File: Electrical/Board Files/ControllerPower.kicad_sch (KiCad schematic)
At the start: 42 parts, among them J1 Conn_01x02_Female, Q1 PJA3411, Q2 PJA3411, SW11 SW_DIP_x01, U1 TPS63020, U2 BQ25050DQCR

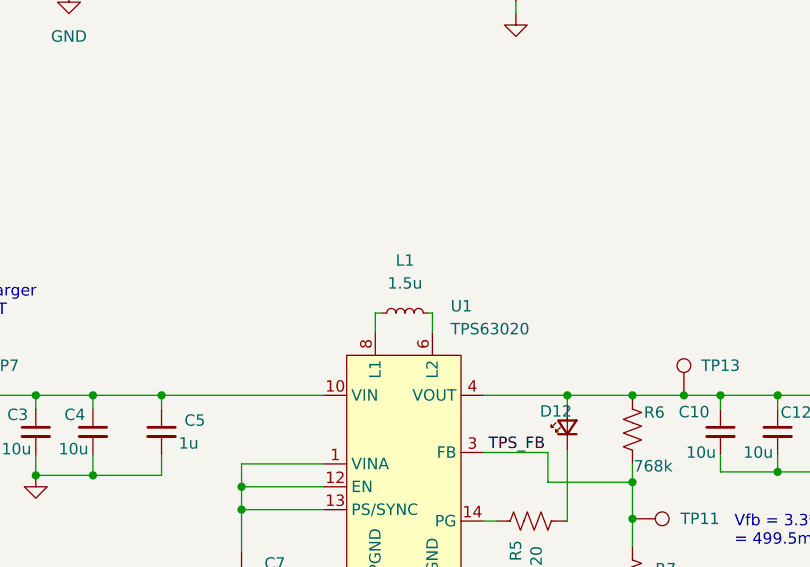
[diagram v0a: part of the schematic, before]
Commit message: Adding some device footprints and MPN
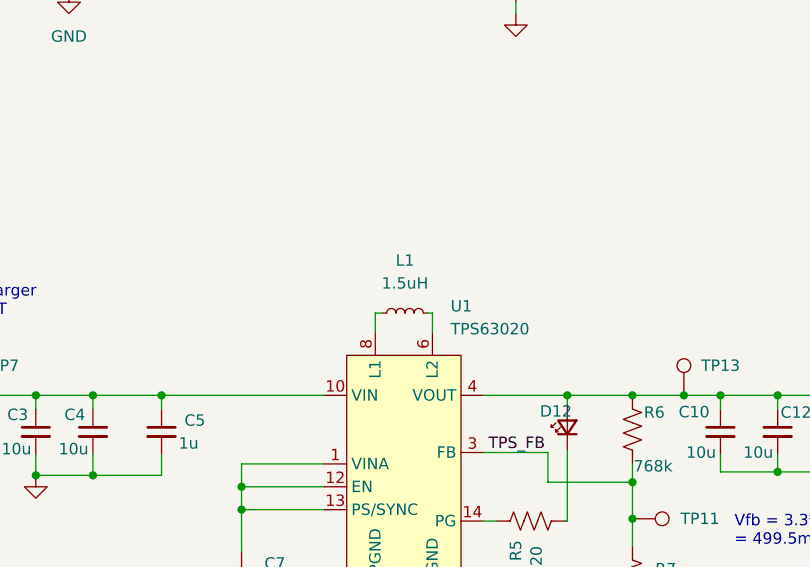
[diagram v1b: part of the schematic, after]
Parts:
- C1, C13, C5, C6: MANUFACTURER (none) -> CL10A105KB8NNNC
- C10, C12, C3, C4: MANUFACTURER (none) -> CL10A106MA8NRNC
- C11, C2, C7, C8, C9: footprint (none) -> Capacitor_SMD:C_0603_1608Metric; MANUFACTURER (none) -> CC0603KRX7R9BB104
- C14, C15, C16: MANUFACTURER (none) -> CL21A226MAYNNNE
- D11, D12: value ~ -> -; footprint (none) -> Diode_SMD:D_SOD-323; MANUFACTURER (none) -> 1N4148WS
- JP1: footprint (none) -> Jumper:SolderJumper-2_P1.3mm_Open_TrianglePad1.0x1.5mm; MANUFACTURER (none) -> -
- L1: value 1.5u -> 1.5uH
- R1, R2: footprint (none) -> RC0603FR-07510RL
- R3, R4, R5, R6, R7, TH1: footprint (none) -> Resistor_SMD:R_0603_1608Metric
- TP10: footprint (none) -> TestPoint:TestPoint_THTPad_2.0x2.0mm_Drill1.0mm
- TP11, TP12, TP13, TP14, TP7, TP8, TP9: value ~ -> TestPoint; footprint (none) -> TestPoint:TestPoint_THTPad_2.0x2.0mm_Drill1.0mm
- U2: footprint (none) -> Package_SON:WSON-10-1EP_2x3mm_P0.5mm_EP0.84x2.4mm_ThermalVias

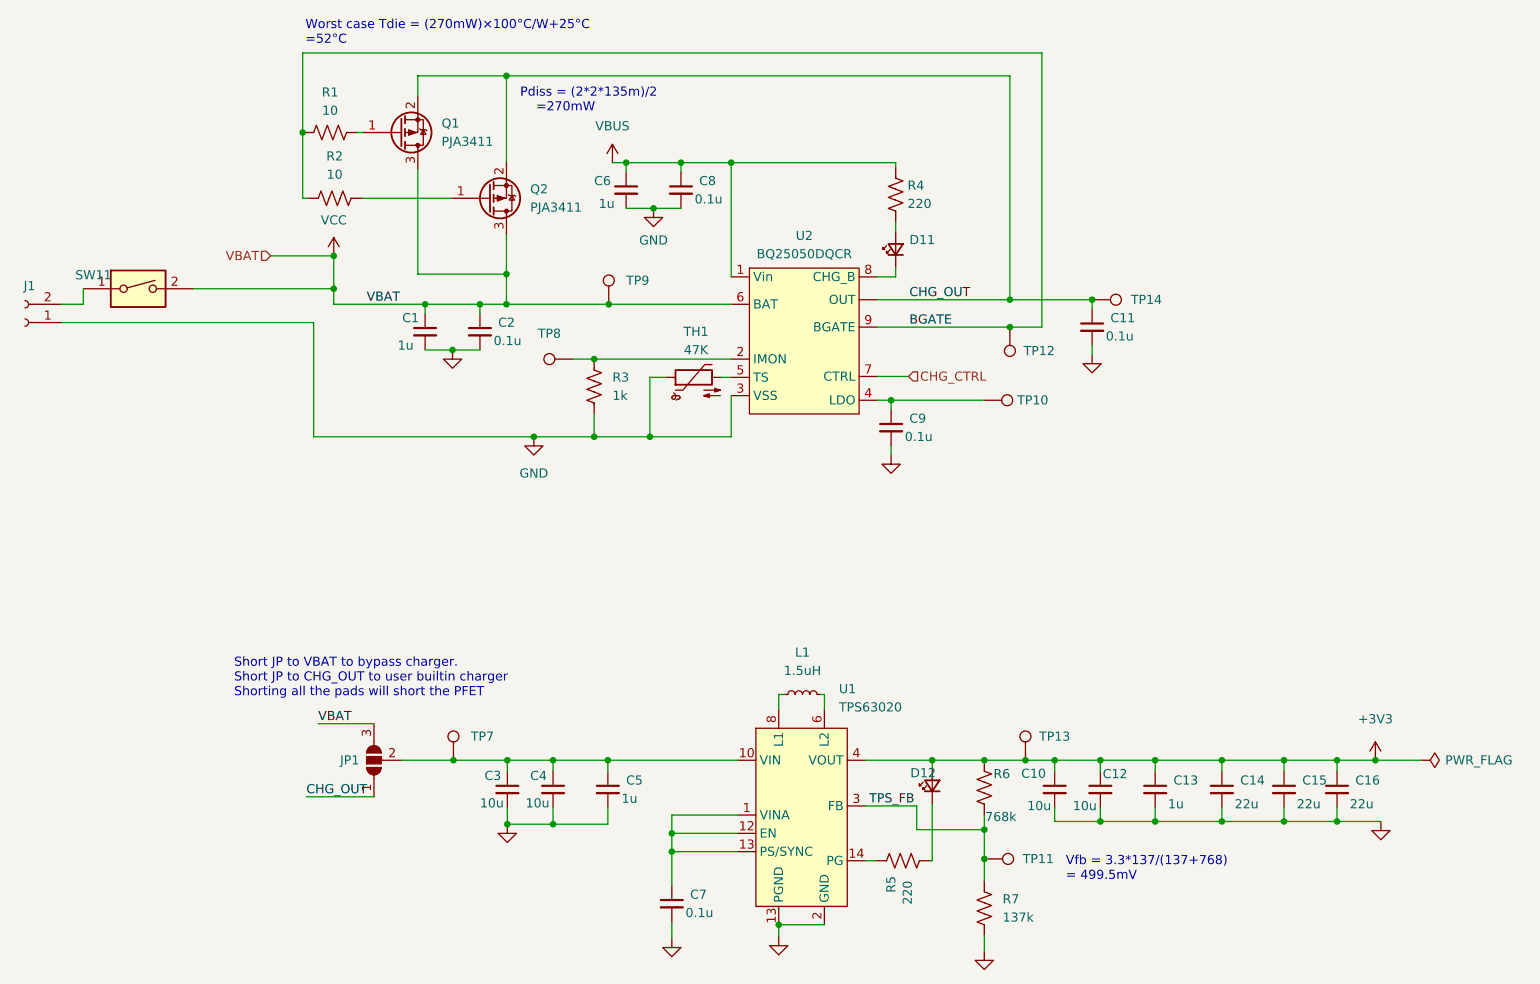
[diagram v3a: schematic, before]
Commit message: Adding footprints
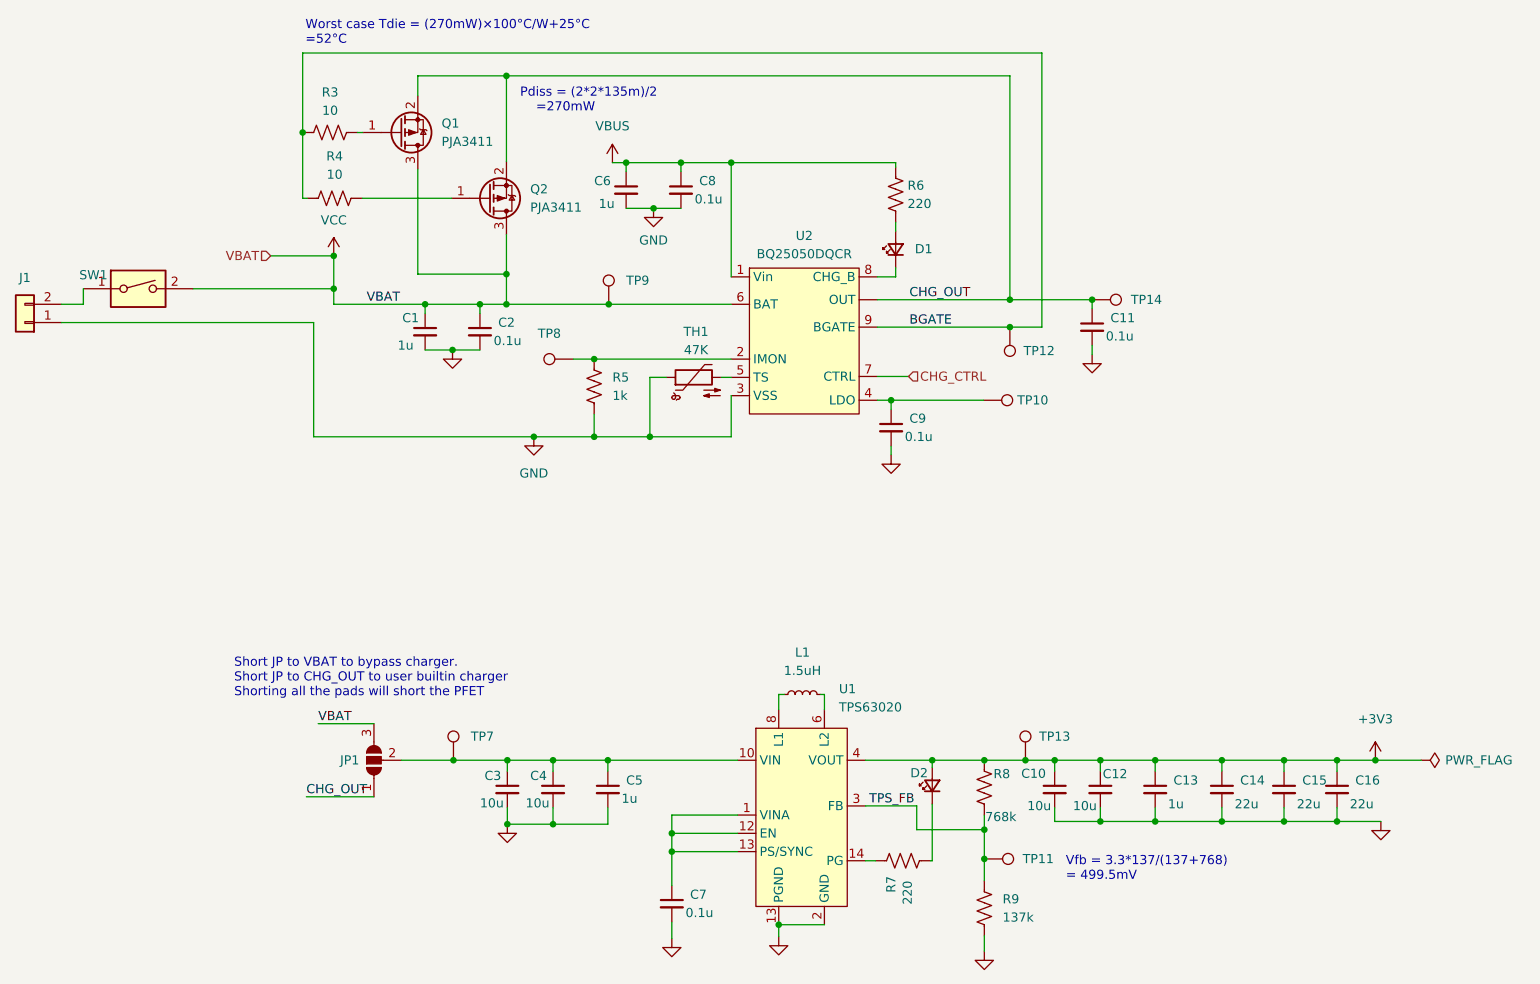
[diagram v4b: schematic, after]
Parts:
- C1, C10, C12, C13, C14, C15, C16, C3, C4, C5, C6: footprint (none) -> Capacitor_SMD:C_0805_2012Metric
- C11, C2, C7, C8, C9: footprint Capacitor_SMD:C_0603_1608Metric -> Capacitor_SMD:C_0805_2012Metric
- D1: renamed from D11; value - -> CHARGE_LED; footprint Diode_SMD:D_SOD-323 -> LED_SMD:LED_0603_1608Metric
- D2: renamed from D12; value - -> PWR_LED; footprint Diode_SMD:D_SOD-323 -> LED_SMD:LED_0603_1608Metric
- J1: value Conn_01x02_Female -> BATT; footprint (none) -> Connector_PinSocket_2.54mm:PinSocket_1x02_P2.54mm_Vertical; symbol Connector:Conn_01x02_Female -> Connector_Generic:Conn_01x02
- L1: footprint (none) -> Connector_PinSocket_2.00mm:PinSocket_1x02_P2.00mm_Vertical
- Q1, Q2: footprint (none) -> Package_TO_SOT_SMD:SOT-23
- R3: renamed from R1; footprint RC0603FR-07510RL -> Resistor_SMD:R_0805_2012Metric
- R4: renamed from R2; footprint RC0603FR-07510RL -> Resistor_SMD:R_0805_2012Metric
- SW1: renamed from SW11; footprint (none) -> Button_Switch_THT:SW_PUSH-12mm
- U1: footprint (none) -> Rocekerrobotics:IC_TPS63020DSJR
- renumbered R3 to R5, R4 to R6, R5 to R7, R6 to R8, R7 to R9
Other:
- moved on the sheet: J1
